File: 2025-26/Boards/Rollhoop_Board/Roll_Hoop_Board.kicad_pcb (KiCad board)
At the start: 2 copper layers, 106.7 x 32 mm, 24 parts, among them J1 DTM13-12PA, J2 DTM13-12PA, Q1 AO3401A, Q2 AO3400A, Q3 AO3400A, U1 AMS1117-3.3, U2 SN65HVD230, U3 STM32C011F4Px

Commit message: Rollhoop edits
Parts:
- added F1: MINISMDC020F-2, MINISMDC020F-2:FUS_MINISMDC020F_TYCO_TYC, F.Cu at (138.5, 39.0)
- added Molex5: 043045-0212, Connector_Molex:Molex_Micro-Fit_3.0_43045-0212_2x01_P3.00mm_Vertical, F.Cu at (140.0, 31.0)
- added Molex6: 043045-0212, Connector_Molex:Molex_Micro-Fit_3.0_43045-0212_2x01_P3.00mm_Vertical, F.Cu at (198.0, 31.0)
- added Q4: AO3400A, Package_TO_SOT_SMD:SOT-23, F.Cu at (150.5, 28.5)
- added Q5: AO3400A, Package_TO_SOT_SMD:SOT-23, F.Cu at (156.0, 28.5)
- U1: value AMS1117-3.3 -> UA78M33QDCYRQ1
- moved Molex3 13.0 mm to (207.0, 37.9)
- moved Molex1 12.5 mm to (217.0, 37.9)
- moved Q2 7.11 mm to (207.5, 28.0), turned to 90 degrees
- moved D2 6.62 mm to (192.0, 37.8)
- moved D1 5.93 mm to (145.5, 37.0)
- moved L2 5.59 mm to (168.0, 37.0)
- moved U1 5.52 mm to (152.7, 35.0)
- moved C1 5.51 mm to (150.5, 40.5)
- moved C2 5.51 mm to (155.5, 40.5)
- moved C5 5.51 mm to (169.5, 33.5)
- moved C3 5.51 mm to (182.4, 37.8)
- moved C4 5.51 mm to (170.4, 37.2)
- moved L1 5.51 mm to (186.4, 37.8)
- moved R2 5.51 mm to (181.9, 40.8)
- moved R3 5.51 mm to (181.9, 34.8)
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- renumbered L3 to L1
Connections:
- J2 pad 4: unconnected-(J2-Pad4) -> DSH_PWR
- J2 pad 5: DSH_PWR -> unconnected-(J2-Pad5)
- Molex1 pad 1: +12V -> Net-(Q1-D)
- Molex3 pad 1: +12V -> Net-(Q1-D)
- Q2 pad 1: Green_LED -> Red_LED
- Q2 pad 3: Green_Out -> Red_Out
- Q3 pad 1: Red_LED -> Green_LED
- Q3 pad 3: Red_Out -> Green_Out
- U1 pad 1: GND -> Net-(Q1-D)
- U1 pad 2: RLH_3.3V -> GND
- U1 pad 3: Net-(Q1-D) -> RLH_3.3V
- U3 pad 1: unconnected-(U3-PB7-Pad1) -> Buzzer2
- U3 pad 2: unconnected-(U3-PC14-Pad2) -> Buzzer1
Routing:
- net DSH_PWR: track 131.9 -> 7.77 mm
- net Net-(Q1-D): track 11.1 -> 107.4 mm
- net DSH_CAN_L: track 12.1 -> 66.4 mm
- net DSH_CAN_H: track 21.4 -> 66.6 mm
- net Buzzer2_Out: track 0.00 -> 43.0 mm
- net DSH_CAN_S: track 93.9 -> 51.5 mm
- net Red_Out: track 28.5 -> 8.08 mm
- net Red_LED: track 71.9 -> 55.2 mm
- net Buzzer1: track 0.00 -> 10.8 mm
- net Net-(Q1-S): track 0.00 -> 7.87 mm
- net Buzzer1_Out: track 0.00 -> 7.60 mm
- net (no net): track 7.14 -> 0.00 mm
- net Buzzer2: track 0.00 -> 6.02 mm
- net RX: track 14.0 -> 9.97 mm, vias 2 -> 0
- net DSH_SDC_IN: track 77.1 -> 81.0 mm
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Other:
- board size 106.7 x 32 mm -> 106.7 x 36 mm

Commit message: rollhoop update
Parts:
- removed Q1: AO3401A, Package_TO_SOT_SMD:SOT-23
- removed Q5: AO3400A, Package_TO_SOT_SMD:SOT-23
- removed U1: UA78M33QDCYRQ1, Package_TO_SOT_SMD:SOT-223-3_TabPin2
- added C7: 4.7μF, Capacitor_SMD:C_0402_1005Metric, F.Cu at (159.0, 41.5)
- added F1: Fuse, Fuse:Fuse_1206_3216Metric, F.Cu at (134.0, 40.5)
- added U4: UA78M33QDCYRQ1, Package_TO_SOT_SMD:TO-252-2, F.Cu at (153.5, 32.5)
- C6: renamed from C5; footprint Capacitor_SMD:C_0603_1608Metric_Pad1.08x0.95mm_HandSolder -> Capacitor_SMD:C_0402_1005Metric
- moved Q4 13.6 mm to (144.0, 40.5), turned to 0 degrees
- renumbered L1 to L3, Q3 to Q2, Q2 to Q3
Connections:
- J2 pad 4: DSH_PWR -> unconnected-(J2-Pad4)
- J2 pad 5: unconnected-(J2-Pad5) -> DSH_PWR
- Molex1 pad 1: Net-(Q1-D) -> +12V
- Molex3 pad 1: Net-(Q1-D) -> +12V
- Molex5 pad 1: DSH_PWR -> +12V
- Molex5 pad 2: Buzzer1_Out -> Speaker_Out
- Molex6 pad 1: Net-(Q1-D) -> +12V
- Molex6 pad 2: Buzzer2_Out -> Speaker_Out
- Q4 pad 1: Buzzer1 -> Speaker
- Q4 pad 3: Buzzer1_Out -> Speaker_Out
- U3 pad 1: Buzzer2 -> unconnected-(U3-PB7-Pad1)
- U3 pad 2: Buzzer1 -> unconnected-(U3-PC14-Pad2)
- U3 pad 9: unconnected-(U3-PA2-Pad9) -> Speaker
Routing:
- net +12V: track 0.00 -> 111.6 mm
- net DSH_PWR: track 7.77 -> 84.7 mm
- net Speaker_Out: track 0.00 -> 74.0 mm
- net Buzzer2_Out: track 43.0 -> 0.00 mm
- net Speaker: track 0.00 -> 41.7 mm, vias 0 -> 2
- net Net-(Q1-D): track 107.4 -> 84.6 mm
- net Buzzer1: track 10.8 -> 0.00 mm
- net Buzzer1_Out: track 7.60 -> 0.00 mm
- net RLH_3.3V: track 29.0 -> 35.2 mm
- net Buzzer2: track 6.02 -> 0.00 mm
- net Net-(Q1-G): track 5.41 -> 2.29 mm
- net unconnected-(U3-PC14-Pad2): track 0.00 -> 0.66 mm
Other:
- board text added: "${REFERENCE}"

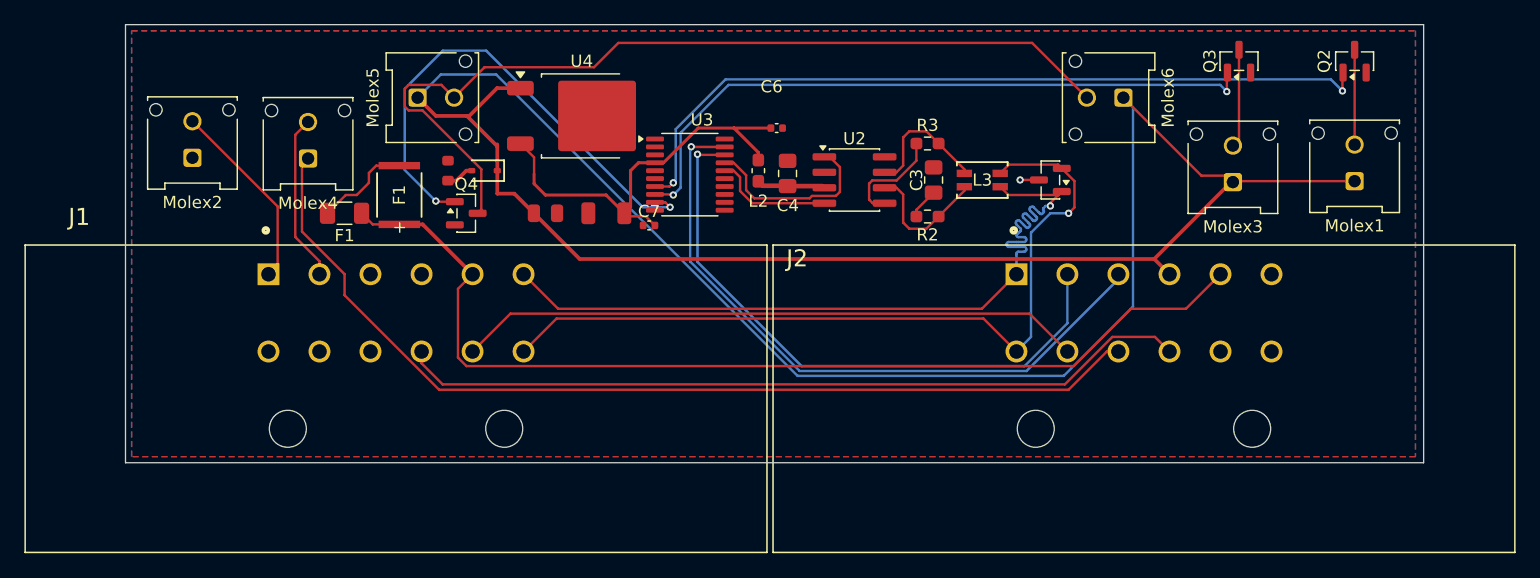
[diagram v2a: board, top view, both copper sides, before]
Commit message: Rollhoop board updates
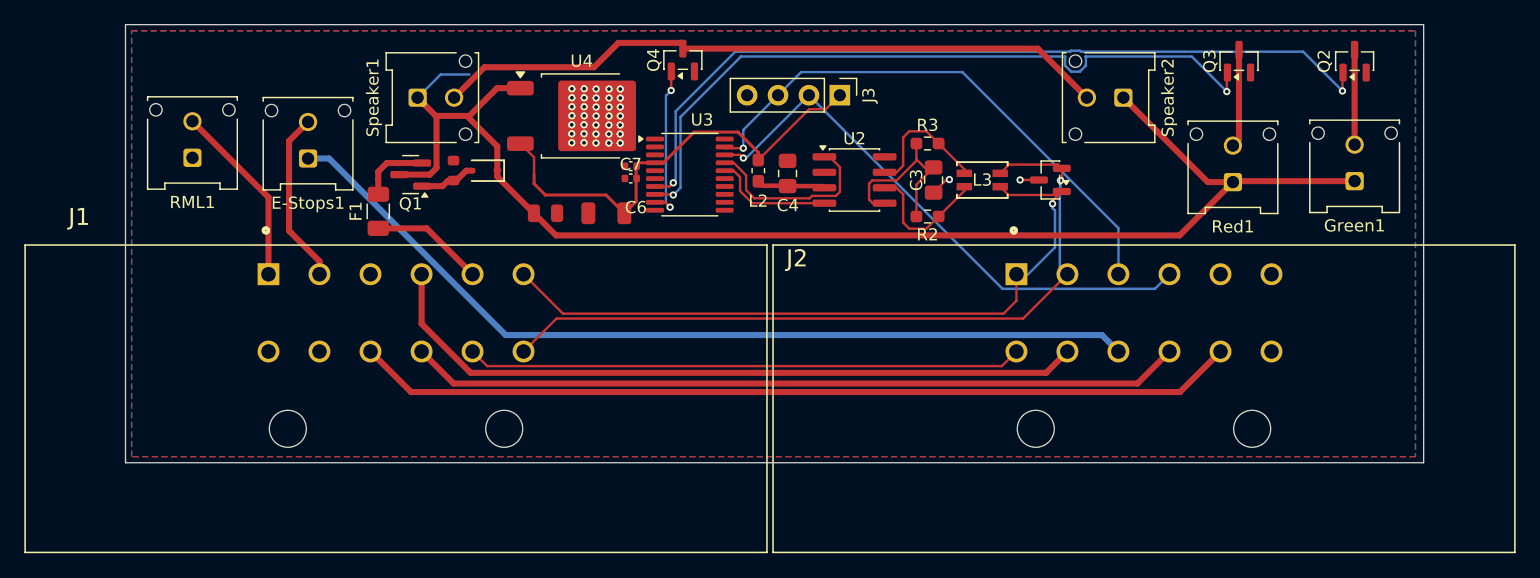
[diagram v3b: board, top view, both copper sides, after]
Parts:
- removed the F1 at (138.5, 39.0)
- added J3: Conn_01x04_Pin, Connector_PinHeader_2.54mm:PinHeader_1x04_P2.54mm_Vertical, F.Cu at (174.7, 30.8)
- added Q1: AO3401A, Package_TO_SOT_SMD:SOT-23, F.Cu at (139.4, 37.3)
- moved Q4 21.8 mm to (161.8, 27.9), turned to 90 degrees
- moved C6 12.4 mm to (157.5, 36.6), turned to 0 degrees
- moved C7 4.14 mm to (157.5, 37.6)
- moved F1 2.77 mm to (136.8, 40.3), turned to 90 degrees
- moved R1 0.45 mm to (142.9, 37.0)
- renumbered Molex4 to E-Stops1, Molex1 to Green1, Molex2 to RML1, Molex3 to Red1, Molex5 to Speaker1, Molex6 to Speaker2
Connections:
- C1 pad 1: Net-(Q1-D) -> +12V
- C3 pad 1: GND -> Vref
- D1 pad 1: Net-(Q1-D) -> +12V
- F1 pad 1: DSH_PWR -> RLH_PWR
- J1 pad 10: unconnected-(J1-Pad10) -> Extra
- J1 pad 4: unconnected-(J1-Pad4) -> DSH_PWR
- J1 pad 5: DSH_PWR -> RLH_PWR
- J2 pad 11: DSH_CAN_S -> DSH_PWR
- J2 pad 12: DSH_CAN_H -> DSH_CAN_S
- J2 pad 2: SWDIO -> DSH_CAN_H
- J2 pad 4: unconnected-(J2-Pad4) -> SWDIO
- J2 pad 5: DSH_PWR -> unconnected-(J2-Pad5)
- J2 pad 8: unconnected-(J2-Pad8) -> Extra
- R2 pad 2: GND -> Vref
- R3 pad 1: GND -> Vref
- U2 pad 5: GND -> Vref
- U4 pad 1: Net-(Q1-D) -> +12V
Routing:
- net Net-(Q1-D): track 84.6 -> 0.00 mm
- net Extra: track 0.00 -> 72.6 mm
- net Speaker: track 41.7 -> 12.9 mm
- net DSH_PWR: track 84.7 -> 59.5 mm
- net Speaker_Out: track 74.0 -> 55.5 mm
- net Vref: track 0.00 -> 15.1 mm
- net GND: track 12.9 -> 3.31 mm, vias 1 -> 37
- net RLH_PWR: track 0.00 -> 9.31 mm
- net SWCLK: track 54.7 -> 45.6 mm
- net DSH_CAN_L: track 66.4 -> 59.0 mm
- net DSH_SDC_IN: track 81.0 -> 73.9 mm
- net DSH_CAN_S: track 51.5 -> 45.7 mm
- net DSH_CAN_H: track 66.6 -> 61.9 mm
- net SWDIO: track 50.5 -> 45.9 mm
- net Red_LED: track 55.2 -> 59.9 mm
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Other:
- board text removed: "${REFERENCE}"

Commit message: Rollhoop board edit
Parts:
- removed Green1, RML1, Red1: 043045-0212, Connector_Molex:Molex_Micro-Fit_3.0_43045-0212_2x01_P3.00mm_Vertical
- added J4: 043045-0612, Connector_Molex:Molex_Micro-Fit_3.0_43045-0612_2x03_P3.00mm_Vertical, F.Cu at (130.1, 37.5)
- added J5: 043045-0612, Connector_Molex:Molex_Micro-Fit_3.0_43045-0612_2x03_P3.00mm_Vertical, F.Cu at (120.1, 37.5)
- E-Stops1: value 043045-0212 -> 043045-0612
- moved Speaker1 77.4 mm to (217.0, 38.5), turned to -90 degrees
- moved Q2 75.5 mm to (141.6, 31.4), turned to 180 degrees
- moved E-Stops1 75.3 mm to (206.0, 29.5), turned to -90 degrees
- moved Q3 66.0 mm to (141.5, 27.5), turned to 180 degrees
- moved Speaker2 9.92 mm to (204.5, 38.5)
- moved F1 7.72 mm to (144.4, 41.5), turned to 180 degrees
- moved R2 3.18 mm to (185.0, 41.5)
- moved R1 2.53 mm to (141.1, 35.3), turned to 0 degrees
- moved Q1 2.47 mm to (141.4, 38.8), turned to -90 degrees
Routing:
- net RLH_SDC_IN: track 14.2 -> 81.6 mm
- net Green_LED: track 67.3 -> 34.9 mm, vias 2 -> 3
- net Red_LED: track 59.9 -> 36.3 mm
- net Red_Out: track 8.08 -> 29.2 mm
- net DSH_SDC_IN: track 73.9 -> 55.9 mm
- net Green_Out: track 7.80 -> 23.1 mm, vias 0 -> 1
- net +12V: track 116.1 -> 123.0 mm
- net RLH_RML_YELLOW: track 15.2 -> 20.2 mm
- net RLH_PWR: track 9.31 -> 4.54 mm
- net Speaker_Out: track 55.5 -> 59.0 mm
- net GND: track 3.31 -> 6.28 mm
- net Net-(Q1-G): track 4.61 -> 5.44 mm
